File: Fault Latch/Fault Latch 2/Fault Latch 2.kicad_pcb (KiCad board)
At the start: 2 copper layers, 110 x 90 mm, 108 parts, among them K101 Fujitsu_FTR-LYAA005x, K102 Fujitsu_FTR-LYAA005x, K103 Fujitsu_FTR-LYAA005x, Q101 Q_NPN_BEC, Q102 Q_NPN_BEC, Q103 Q_NPN_BEC, Q104 Q_NPN_BEC, Q105 Q_NMOS_GSD, Q106 Q_NMOS_GSD, Q107 Q_PMOS_GSD, Q108 Q_PMOS_GSD, Q109 Q_NMOS_GDS, Q110 Q_NPN_BEC, Q111 Q_NPN_BEC, Q112 Q_NMOS_GSD, Q113 Q_PMOS_GSD, SW101 SW_Omron_B3FS, SW102 SW_Omron_B3FS, SW103 SW_Omron_B3FS, U101 SFH617A-1, U102 SFH617A-1, U103 SFH617A-1, U104 74AHC1G00, U105 74AHC1G00, U106 74AHC1G00, U107 74LS279, U108 641964-1, U109 SFH617A-1, U110 SFH617A-1, U111 641964-1, U112 641964-1, U113 641964-1, U114 641964-1, U115 641964-1, U116 641964-1, U117 74AHC1G00, U118 LM555xM, U119 74AHC1G00, U120 641964-1, U121 SFH617A-1, U122 641964-1

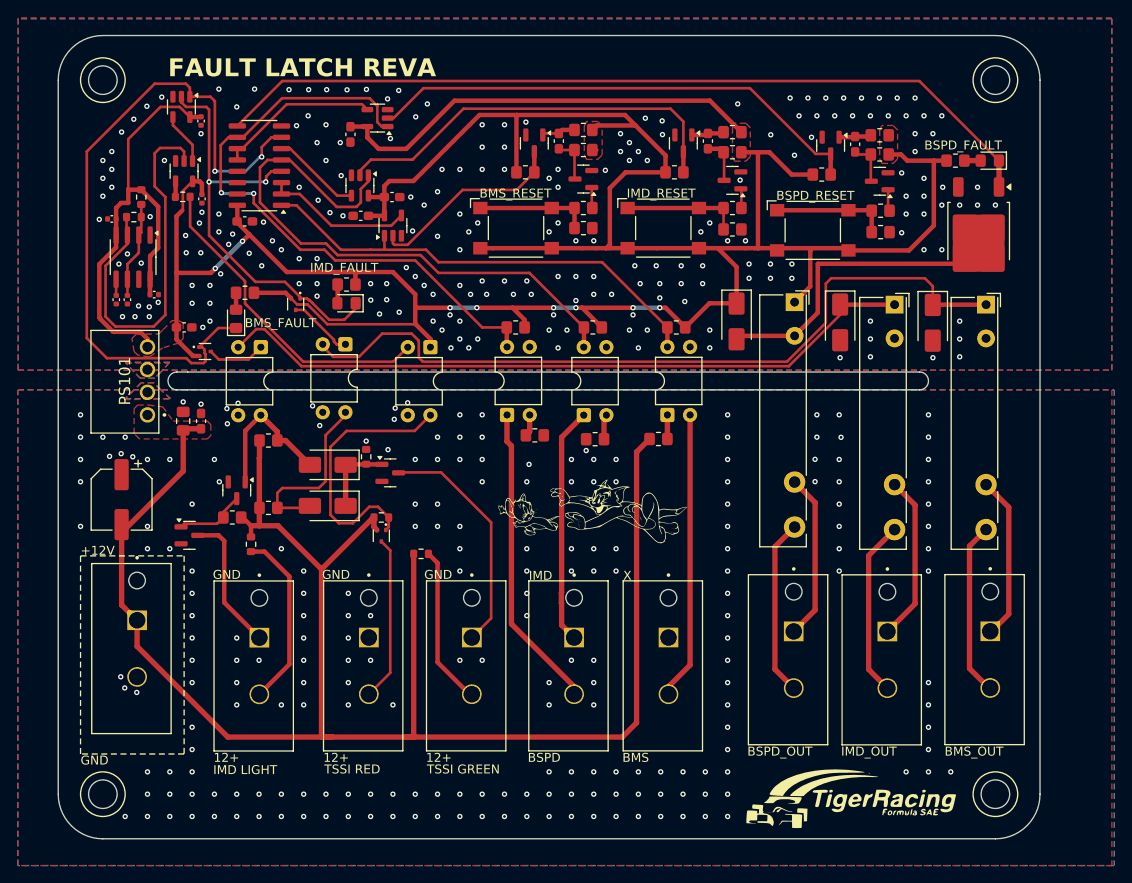
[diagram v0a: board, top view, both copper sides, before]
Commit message: BSPD now active low output, fault latch rerouted.
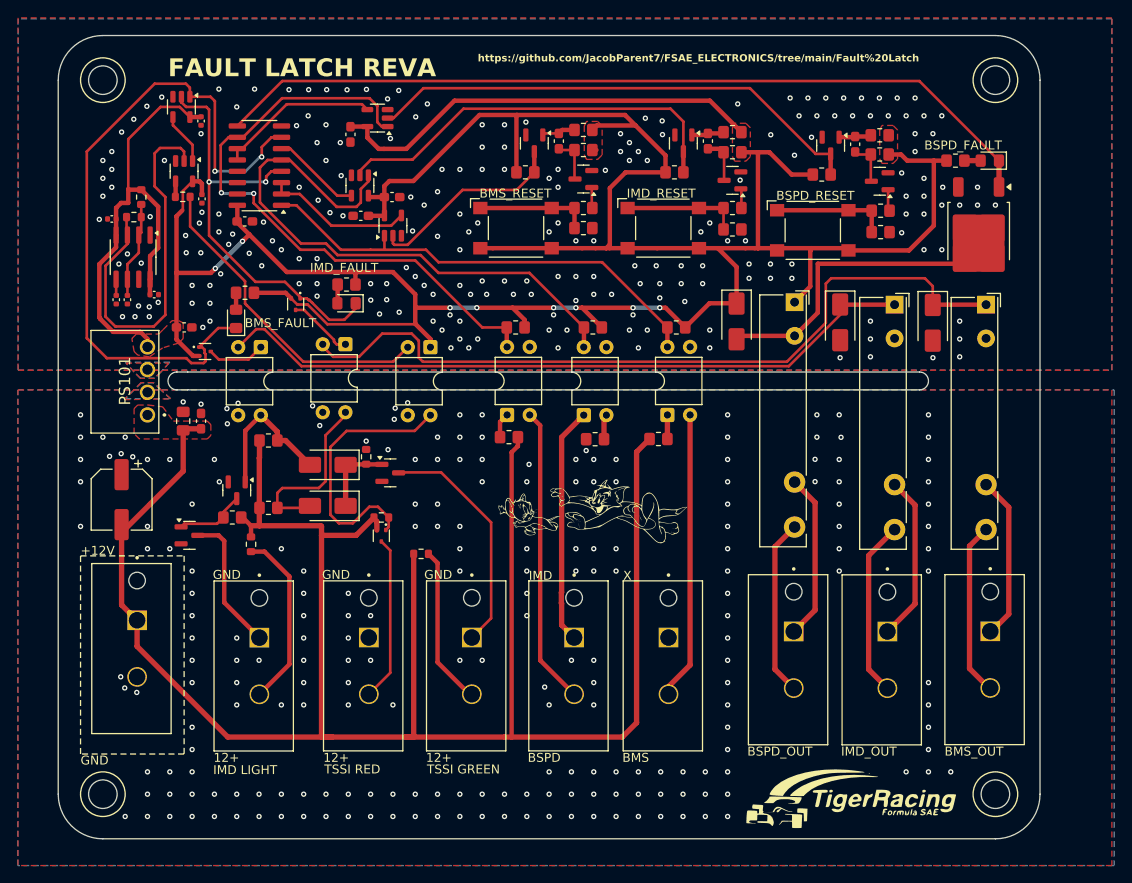
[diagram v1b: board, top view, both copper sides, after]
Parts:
- moved R104 2.91 mm to (119.7, 89.1), turned to 0 degrees
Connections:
- R104 pad 1: GNDPWR -> Net-(R104-Pad1)
- R104 pad 2: Net-(R104-Pad2) -> +12V
- U103 pad 1: /BSPD_HV -> Net-(R104-Pad1)
- U103 pad 2: Net-(R104-Pad2) -> /BSPD_HV
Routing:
- net +12V: track 196.6 -> 231.8 mm
- net Net-(R104-Pad1): track 0.00 -> 2.83 mm
- net Net-(R104-Pad2): track 2.53 -> 0.00 mm
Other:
- board text added: "https://github.com/JacobParent7/FSAE_ELECTRONICS/tree/main/Fault%20Latch"
